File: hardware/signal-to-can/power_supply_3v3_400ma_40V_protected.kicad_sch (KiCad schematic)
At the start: 10 parts

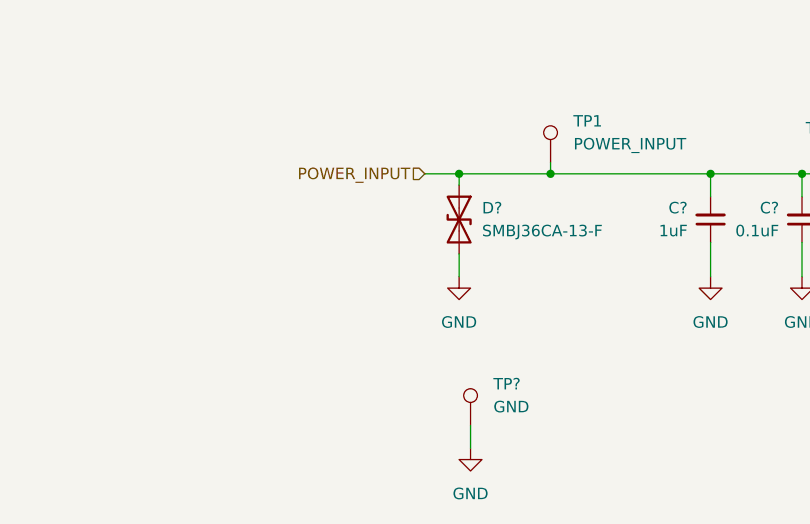
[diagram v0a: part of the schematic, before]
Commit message: AFE, power supply, connector
Ready for PCB layout
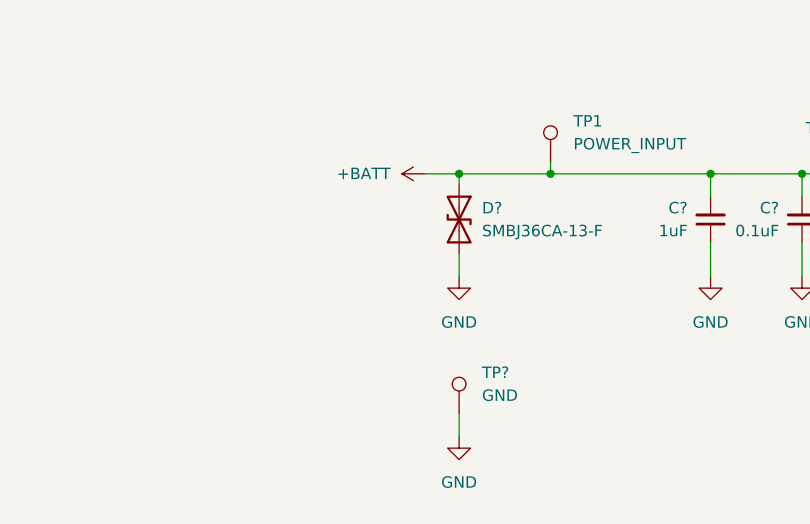
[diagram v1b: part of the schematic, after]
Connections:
- net POWER_INPUT renamed +BATT
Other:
- moved on the sheet: TP?
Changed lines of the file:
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@@
 	(wire
 		(pts
-			(xy 116.84 119.38) (xy 116.84 121.92)
+			(xy 115.57 118.11) (xy 115.57 120.65)
 		)
 		(stroke
@@
 		)
 	)
-	(hierarchical_label "POWER_INPUT"
-		(shape input)
-		(at 111.76 91.44 180)
-		(effects
-			(font
-				(size 1.27 1.27)
-			)
-			(justify right)
-		)
-	)
 	(symbol
 		(lib_id "power:GND")
@@
 				(path "/e63e39d7-6ac0-4ffd-8aa3-1841a4541b55/b68ab937-188e-4e6d-8c94-721c05c291d6"
 					(reference "R8")
+					(unit 1)
+				)
+			)
+		)
+	)
+	(symbol
+		(lib_id "power:+BATT")
+		(at 111.76 91.44 90)
+		(unit 1)
+		(exclude_from_sim no)
+		(in_bom yes)
+		(on_board yes)
+		(dnp no)
+		(fields_autoplaced yes)
+		(property "Reference" "#PWR049"
+			(at 115.57 91.44 0)
+			(effects
+				(font
+					(size 1.27 1.27)
+				)
+				(hide yes)
+			)
+		)
+		(property "Value" "+BATT"
+			(at 107.95 91.4399 90)
+			(effects
+				(font
+					(size 1.27 1.27)
+				)
+				(justify left)
+			)
+		)
+		(property "Footprint" ""
+			(at 111.76 91.44 0)
+			(effects
+				(font
+					(size 1.27 1.27)
+				)
+				(hide yes)
+			)
+		)
+		(property "Datasheet" ""
+			(at 111.76 91.44 0)
+			(effects
+				(font
+					(size 1.27 1.27)
+				)
+				(hide yes)
+			)
+		)
+		(property "Description" "Power symbol creates a global label with name \"+BATT\""
+			(at 111.76 91.44 0)
+			(effects
+				(font
+					(size 1.27 1.27)
+				)
+				(hide yes)
+			)
+		)
+		(pin "1"
+		)
+		(instances
+			(project ""
+				(path "/742f64ac-c4d8-4561-a2a9-e0e3f6f67ce8/7b74f6f5-1560-4843-a54e-584b3d17c5b1"
+					(reference "#PWR049")
 					(unit 1)
 				)
@@
 	(symbol
 		(lib_id "power:GND")
-		(at 116.84 121.92 0)
+		(at 115.57 120.65 0)
 		(unit 1)
 		(exclude_from_sim no)
@@
 		(fields_autoplaced yes)
 		(property "Reference" "#PWR?"
-			(at 116.84 128.27 0)
+			(at 115.57 127 0)
 			(effects
 				(font
@@
 		)
 		(property "Value" "GND"
-			(at 116.84 127 0)
+			(at 115.57 125.73 0)
 			(effects
 				(font
@@
 		)
 		(property "Footprint" ""
-			(at 116.84 121.92 0)
+			(at 115.57 120.65 0)
 			(effects
 				(font
@@
 		)
 		(property "Datasheet" ""
-			(at 116.84 121.92 0)
-			(effects
-				(font
-					(size 1.27 1.27)
-				)
-				(hide yes)
-			)
-		)
-		(property "Description" ""
-			(at 116.84 121.92 0)
+			(at 115.57 120.65 0)
+			(effects
+				(font
+					(size 1.27 1.27)
+				)
+				(hide yes)
+			)
+		)
+		(property "Description" ""
+			(at 115.57 120.65 0)
 			(effects
 				(font
@@
 	(symbol
 		(lib_id "Connector:TestPoint")
-		(at 116.84 119.38 0)
+		(at 115.57 118.11 0)
 		(unit 1)
 		(exclude_from_sim no)
@@
 		(fields_autoplaced yes)
 		(property "Reference" "TP?"
-			(at 119.38 114.8079 0)
+			(at 118.11 113.5379 0)
 			(effects
 				(font
@@
 		)
 		(property "Value" "GND"
-			(at 119.38 117.3479 0)
+			(at 118.11 116.0779 0)
 			(effects
 				(font
@@
 		)
 		(property "Footprint" "TestPoint:TestPoint_Pad_D2.0mm"
-			(at 121.92 119.38 0)
+			(at 120.65 118.11 0)
 			(effects
 				(font
@@
 		)
 		(property "Datasheet" "~"
-			(at 121.92 119.38 0)
-			(effects
-				(font
-					(size 1.27 1.27)
-				)
-				(hide yes)
-			)
-		)
-		(property "Description" ""
-			(at 116.84 119.38 0)
-			(effects
-				(font
+			(at 120.65 118.11 0)
+			(effects
+				(font
+					(size 1.27 1.27)
+				)
+				(hide yes)
+			)
+		)
+		(property "Description" ""
+			(at 115.57 118.11 0)
+			(effects
+				(font

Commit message: 1st rev PCB layout
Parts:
- removed D?: SMBJ36CA-13-F, Diode_SMD:D_SMB, symbol Device:D_TVS
- TP1: footprint TestPoint:TestPoint_Pad_D2.0mm -> TestPoint:TestPoint_Pad_D1.0mm
- TP2, TP3: renamed from TP?; footprint TestPoint:TestPoint_Pad_D2.0mm -> TestPoint:TestPoint_Pad_D1.0mm
- gave numbers to parts that had none: 6
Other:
- moved on the sheet: TP2
